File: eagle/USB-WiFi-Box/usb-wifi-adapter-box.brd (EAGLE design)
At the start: 86.4 x 52.1 mm, 12 parts

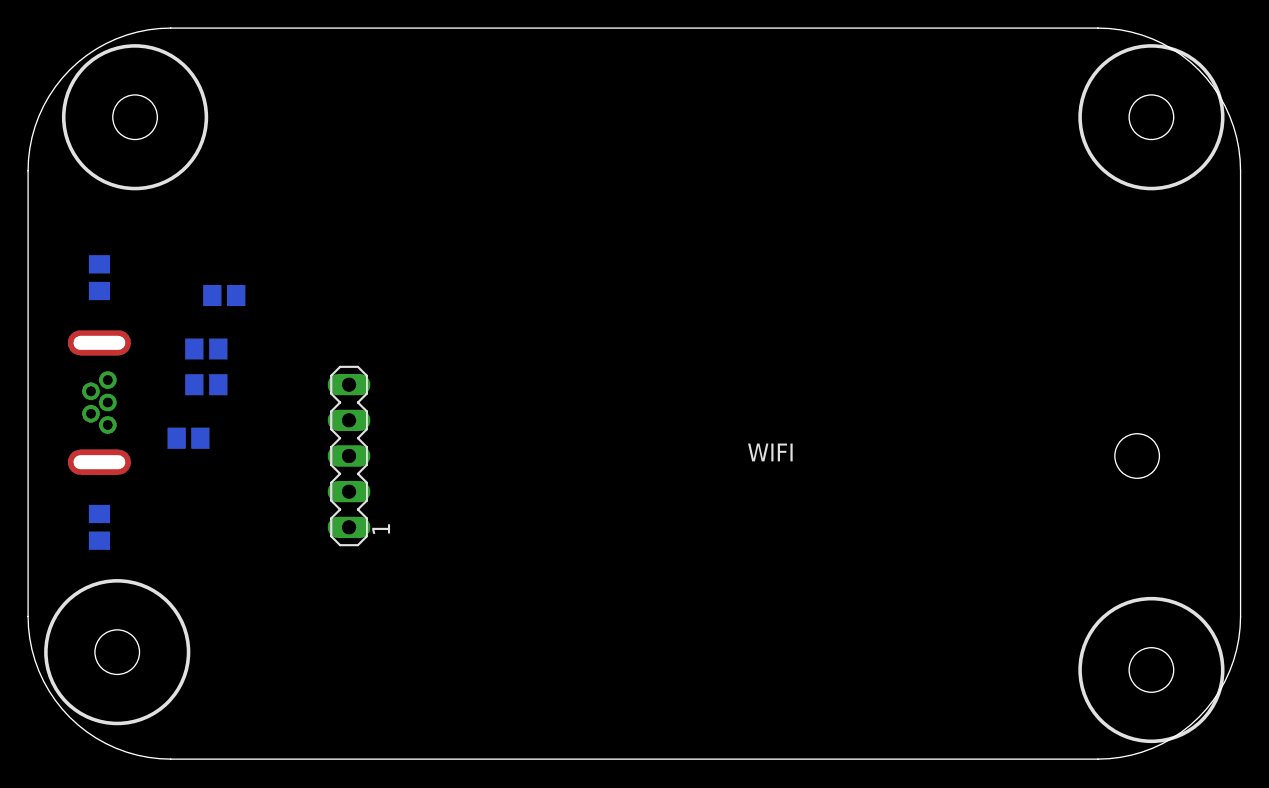
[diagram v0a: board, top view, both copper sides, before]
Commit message: board layout v1, using one wire for VCC, fixed slots in USB part
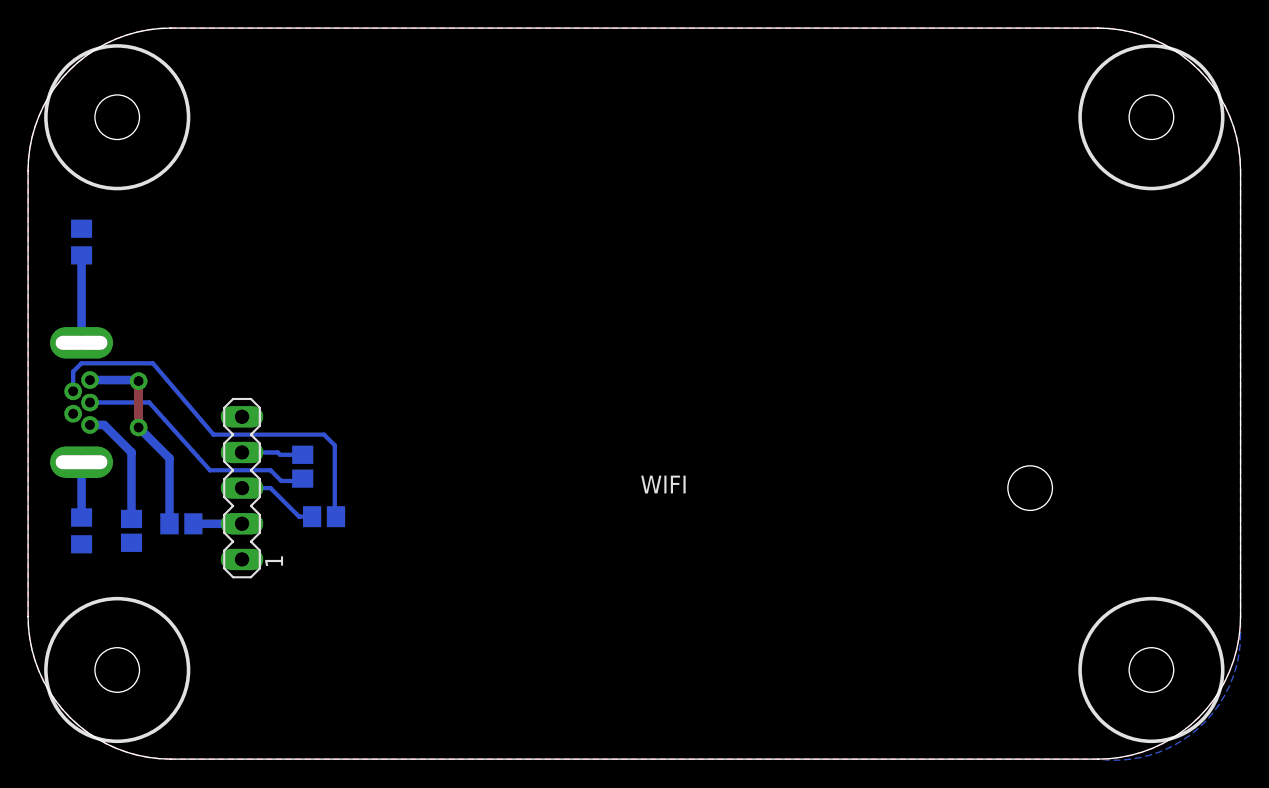
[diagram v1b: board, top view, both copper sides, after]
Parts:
- moved L1 18.0 mm to (7.37, 16.3), turned to 270 degrees
- moved L3 12.6 mm to (21.1, 17.3)
- moved L4 10.8 mm to (19.6, 20.8), turned to 90 degrees
- moved WIFI 7.96 mm to (44.5, 19.3)
- moved L2 6.12 mm to (10.9, 16.8)
- moved C1 2.84 mm to (3.81, 36.8), turned to 90 degrees
- moved C2 1.30 mm to (3.81, 16.3), turned to 270 degrees
- moved FOOT1 1.27 mm to (6.35, 45.7)
- moved FOOT2 1.27 mm to (6.35, 6.35)
- moved CONN1 1.27 mm to (3.81, 25.4)
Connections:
- net N$10 renamed D+
- net N$3 renamed D+OUT
- net N$4 renamed D-OUT
- net N$5 renamed VCC_OUT
- net N$6 renamed GNDOUT
- net N$8 renamed VCC
- net N$9 renamed D-
- removed net N$1: C2.1, CONN1.SLT2
- removed net N$7: C1.1, CONN1.SLT1
- new net SHEILDGND1: C2.1, CONN1.SHLD@2
- new net SHIELDGND2: C1.1, CONN1.SHLD@1
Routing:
- net D-OUT: track 0.00 -> 28.1 mm
- net D+OUT: track 0.00 -> 17.7 mm
- net VCC_OUT: track 0.00 -> 14.6 mm, vias 0 -> 2
- net GNDOUT: track 0.00 -> 8.50 mm
- net SHIELDGND2: track 0.00 -> 6.23 mm
- net D-: track 0.00 -> 5.83 mm
- net D+: track 0.00 -> 4.39 mm
- net SHEILDGND1: track 0.00 -> 3.94 mm
- net VCC: track 0.00 -> 3.47 mm
- added copper zone on layer 1, net GND
- added copper zone on layer 16, net GND
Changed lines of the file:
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@@
 <setting verticaltext="up"/>
 </settings>
-<grid distance="0.1" unitdist="inch" unit="inch" style="lines" multiple="1" display="yes" altdistance="0.025" altunitdist="inch" altunit="inch"/>
+<grid distance="0.01" unitdist="inch" unit="inch" style="lines" multiple="1" display="yes" altdistance="0.025" altunitdist="inch" altunit="inch"/>
 <layers>
-<layer number="1" name="Top" color="4" fill="1" visible="yes" active="yes"/>
+<layer number="1" name="Top" color="4" fill="1" visible="no" active="yes"/>
 <layer number="16" name="Bottom" color="1" fill="1" visible="yes" active="yes"/>
 <layer number="17" name="Pads" color="2" fill="1" visible="yes" active="yes"/>
@@
 <layer number="44" name="Drills" color="7" fill="1" visible="no" active="yes"/>
 <layer number="45" name="Holes" color="7" fill="1" visible="no" active="yes"/>
-<layer number="46" name="Milling" color="3" fill="1" visible="no" active="yes"/>
+<layer number="46" name="Milling" color="3" fill="1" visible="yes" active="yes"/>
 <layer number="47" name="Measures" color="7" fill="1" visible="no" active="yes"/>
 <layer number="48" name="Document" color="7" fill="1" visible="yes" active="yes"/>
@@
 </autorouter>
 <elements>
-<element name="CONN1" library="dxwifi" package="RUGGEDUSB" value="MINI-USB_SHIELD" x="5.08" y="25.4" rot="R270"/>
-<element name="L1" library="dxwifi" package="R0805" value="" x="13.97" y="33.02" rot="MR180"/>
-<element name="L4" library="dxwifi" package="R0805" value="" x="12.7" y="29.21" rot="MR0"/>
-<element name="L3" library="dxwifi" package="R0805" value="" x="12.7" y="26.67" rot="MR0"/>
-<element name="L2" library="dxwifi" package="R0805" value="" x="11.43" y="22.86" rot="MR180"/>
-<element name="C1" library="rcl" package="C0805" value="" x="5.08" y="34.29" rot="MR270"/>
-<element name="C2" library="rcl" package="C0805" value="" x="5.08" y="16.51" rot="MR90"/>
-<element name="FOOT1" library="mount-2" package="_4/.400-BARE+STD_TOOL_CLEARANCE" value="_4-BARE_MOUNTING_HOLE/.400" x="7.62" y="45.72" smashed="yes"/>
-<element name="FOOT2" library="mount-2" package="_4/.400-BARE+STD_TOOL_CLEARANCE" value="_4-BARE_MOUNTING_HOLE/.400" x="6.35" y="7.62" smashed="yes"/>
+<element name="CONN1" library="dxwifi" package="RUGGEDUSB" value="MINI-USB_SHIELD" x="3.81" y="25.4" smashed="yes" rot="R270"/>
+<element name="L1" library="dxwifi" package="R0805" value="" x="7.366" y="16.256" rot="MR270"/>
+<element name="L4" library="dxwifi" package="R0805" value="" x="19.558" y="20.828" smashed="yes" rot="MR90">
+<attribute name="NAME" x="19.05" y="23.876" size="1.27" layer="26" rot="MR90"/>
+<attribute name="VALUE" x="17.272" y="20.066" size="1.27" layer="28" rot="MR90"/>
+</element>
+<element name="L3" library="dxwifi" package="R0805" value="" x="21.082" y="17.272" smashed="yes" rot="MR0">
+<attribute name="NAME" x="25.4" y="16.764" size="1.27" layer="26" rot="MR0"/>
+<attribute name="VALUE" x="21.844" y="14.986" size="1.27" layer="28" rot="MR0"/>
+</element>
+<element name="L2" library="dxwifi" package="R0805" value="" x="10.922" y="16.764" rot="MR180"/>
+<element name="C1" library="rcl" package="C0805" value="" x="3.81" y="36.83" rot="MR90"/>
+<element name="C2" library="rcl" package="C0805" value="" x="3.81" y="16.256" rot="MR270"/>
+<element name="FOOT1" library="mount-2" package="_4/.400-BARE+STD_TOOL_CLEARANCE" value="_4-BARE_MOUNTING_HOLE/.400" x="6.35" y="45.72" smashed="yes"/>
+<element name="FOOT2" library="mount-2" package="_4/.400-BARE+STD_TOOL_CLEARANCE" value="_4-BARE_MOUNTING_HOLE/.400" x="6.35" y="6.35" smashed="yes"/>
 <element name="FOOT3" library="mount-2" package="_4/.400-BARE+STD_TOOL_CLEARANCE" value="_4-BARE_MOUNTING_HOLE/.400" x="80.01" y="6.35" smashed="yes"/>
 <element name="FOOT4" library="mount-2" package="_4/.400-BARE+STD_TOOL_CLEARANCE" value="_4-BARE_MOUNTING_HOLE/.400" x="80.01" y="45.72" smashed="yes"/>
-<element name="WIFI" library="dxwifi" package="ZCN-722M" value="ZCN-722M" x="52.07" y="21.59"/>
+<element name="WIFI" library="dxwifi" package="ZCN-722M" value="ZCN-722M" x="44.45" y="19.304"/>
 </elements>
 <signals>
-<signal name="N$3">
+<signal name="D+OUT">
 <contactref element="CONN1" pad="3"/>
 <contactref element="L4" pad="1"/>
-<wire x1="5.68" y1="25.4" x2="13.55" y2="29.21" width="0" layer="19" extent="1-1"/>
-</signal>
-<signal name="N$4">
+<wire x1="4.41" y1="25.4" x2="8.636" y2="25.4" width="0.3048" layer="16"/>
+<wire x1="8.636" y1="25.4" x2="12.954" y2="20.574" width="0.3048" layer="16"/>
+<wire x1="12.954" y1="20.574" x2="17.272" y2="20.574" width="0.3048" layer="16"/>
+<wire x1="17.272" y1="20.574" x2="18.034" y2="19.812" width="0.3048" layer="16"/>
+<wire x1="18.034" y1="19.812" x2="19.392" y2="19.812" width="0.3048" layer="16"/>
+<wire x1="19.392" y1="19.812" x2="19.558" y2="19.978" width="0.3048" layer="16"/>
+</signal>
+<signal name="D-OUT">
 <contactref element="CONN1" pad="2"/>
 <contactref element="L3" pad="1"/>
-<wire x1="4.48" y1="26.2" x2="13.55" y2="26.67" width="0" layer="19" extent="1-1"/>
-</signal>
-<signal name="N$5">
+<wire x1="3.21" y1="26.2" x2="3.21" y2="27.594" width="0.3048" layer="16"/>
+<wire x1="3.21" y1="27.594" x2="3.81" y2="28.194" width="0.3048" layer="16"/>
+<wire x1="3.81" y1="28.194" x2="8.89" y2="28.194" width="0.3048" layer="16"/>
+<wire x1="8.89" y1="28.194" x2="13.208" y2="23.114" width="0.3048" layer="16"/>
+<wire x1="13.208" y1="23.114" x2="21.082" y2="23.114" width="0.3048" layer="16"/>
+<wire x1="21.082" y1="23.114" x2="21.844" y2="22.352" width="0.3048" layer="16"/>
+<wire x1="21.844" y1="22.352" x2="21.844" y2="17.36" width="0.3048" layer="16"/>
+<wire x1="21.844" y1="17.36" x2="21.932" y2="17.272" width="0.3048" layer="16"/>
+</signal>
+<signal name="VCC_OUT">
 <contactref element="CONN1" pad="1"/>
 <contactref element="L2" pad="1"/>
-<wire x1="5.68" y1="27" x2="10.58" y2="22.86" width="0" layer="19" extent="1-1"/>
+<wire x1="10.072" y1="16.764" x2="10.072" y2="21.424" width="0.6096" layer="16"/>
+<wire x1="10.072" y1="21.424" x2="7.874" y2="23.622" width="0.6096" layer="16"/>
+<via x="7.874" y="23.622" extent="1-16" drill="0.7" diameter="1.27"/>
+<wire x1="7.874" y1="23.622" x2="7.874" y2="26.924" width="0.6096" layer="1"/>
+<via x="7.874" y="26.924" extent="1-16" drill="0.7" diameter="1.27"/>
+<wire x1="7.874" y1="26.924" x2="7.798" y2="27" width="0.6096" layer="16"/>
+<wire x1="7.798" y1="27" x2="4.41" y2="27" width="0.6096" layer="16"/>
 </signal>
 <signal name="GND">
@@
 <contactref element="L1" pad="2"/>
 <contactref element="WIFI" pad="5"/>
-<wire x1="14.82" y1="33.02" x2="22.86" y2="26.67" width="0" layer="19" extent="1-1"/>
-<wire x1="5.08" y1="17.46" x2="14.82" y2="33.02" width="0" layer="19" extent="1-1"/>
-<wire x1="5.08" y1="33.34" x2="5.08" y2="17.46" width="0" layer="19" extent="1-1"/>
-</signal>
-<signal name="N$6">
+<polygon width="0.4064" layer="16" orphans="yes">
+<vertex x="0" y="41.91" curve="-90"/>
+<vertex x="10.16" y="52.07"/>
+<vertex x="76.2" y="52.07" curve="-90"/>
+<vertex x="86.36" y="41.91"/>
+<vertex x="86.36" y="8.89" curve="-97.62815"/>
+<vertex x="76.2" y="0"/>
+<vertex x="10.16" y="0" curve="-90"/>
+<vertex x="0" y="10.16"/>
+</polygon>
+<polygon width="0.4064" layer="1">
+<vertex x="0" y="41.91" curve="-90"/>
+<vertex x="10.16" y="52.07"/>
+<vertex x="76.2" y="52.07" curve="-90"/>
+<vertex x="86.36" y="41.91"/>
+<vertex x="86.36" y="10.16" curve="-90"/>
+<vertex x="76.2" y="0"/>
+<vertex x="10.16" y="0" curve="-90"/>
+<vertex x="0" y="10.16"/>
+</polygon>
+</signal>
+<signal name="GNDOUT">
 <contactref element="CONN1" pad="5"/>
 <contactref element="L1" pad="1"/>
-<wire x1="13.12" y1="33.02" x2="5.68" y2="23.8" width="0" layer="19" extent="1-1"/>
-</signal>
-<signal name="N$1">
-<contactref element="CONN1" pad="SLT2"/>
+<wire x1="4.41" y1="23.8" x2="5.41" y2="23.8" width="0.6096" layer="16"/>
+<wire x1="5.41" y1="23.8" x2="7.366" y2="21.844" width="0.6096" layer="16"/>
+<wire x1="7.366" y1="21.844" x2="7.366" y2="17.106" width="0.6096" layer="16"/>
+</signal>
+<signal name="SHEILDGND1">
+<contactref element="CONN1" pad="SHLD@2"/>
 <contactref element="C2" pad="1"/>
-<wire x1="5.08" y1="15.56" x2="5.08" y2="21.15" width="0" layer="19" extent="1-1"/>
-</signal>
-<signal name="N$7">
-<contactref element="CONN1" pad="SLT1"/>
+<wire x1="3.81" y1="17.206" x2="3.81" y2="21.15" width="0.6096" layer="16"/>
+</signal>
+<signal name="SHIELDGND2">
+<contactref element="CONN1" pad="SHLD@1"/>
 <contactref element="C1" pad="1"/>
-<wire x1="5.08" y1="35.24" x2="5.08" y2="29.65" width="0" layer="19" extent="1-1"/>
-</signal>
-<signal name="N$8">
+<wire x1="3.81" y1="35.88" x2="3.81" y2="29.65" width="0.6096" layer="16"/>
+</signal>
+<signal name="VCC">
 <contactref element="L2" pad="2"/>
 <contactref element="WIFI" pad="2"/>
-<wire x1="12.28" y1="22.86" x2="22.86" y2="19.05" width="0" layer="19" extent="1-1"/>
-</signal>
-<signal name="N$9">
+<wire x1="11.772" y1="16.764" x2="15.24" y2="16.764" width="0.6096" layer="16"/>
+</signal>
+<signal name="D-">
 <contactref element="L3" pad="2"/>
 <contactref element="WIFI" pad="3"/>
-<wire x1="11.85" y1="26.67" x2="22.86" y2="21.59" width="0" layer="19" extent="1-1"/>
-</signal>
-<signal name="N$10">
+<wire x1="20.232" y1="17.272" x2="19.304" y2="17.272" width="0.3048" layer="16"/>
+<wire x1="19.304" y1="17.272" x2="17.272" y2="19.304" width="0.3048" layer="16"/>
+<wire x1="17.272" y1="19.304" x2="15.24" y2="19.304" width="0.3048" layer="16"/>
+</signal>
+<signal name="D+">
 <contactref element="L4" pad="2"/>
 <contactref element="WIFI" pad="4"/>
-<wire x1="11.85" y1="29.21" x2="22.86" y2="24.13" width="0" layer="19" extent="1-1"/>
+<wire x1="19.558" y1="21.678" x2="17.946" y2="21.678" width="0.3048" layer="16"/>
+<wire x1="17.946" y1="21.678" x2="17.78" y2="21.844" width="0.3048" layer="16"/>
+<wire x1="17.78" y1="21.844" x2="15.24" y2="21.844" width="0.3048" layer="16"/>
 </signal>
 </signals>

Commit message: fix routing issues
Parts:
- added TP1: PTR1PAD1-13, testpad:P1-13
- moved L3 16.4 mm to (8.64, 27.9), turned to 180 degrees
- moved L4 11.2 mm to (8.38, 21.6), turned to 180 degrees
- moved L1 10.4 mm to (1.27, 24.6), turned to 90 degrees
- moved L2 9.60 mm to (7.62, 25.8)
- moved C1 3.94 mm to (3.81, 32.9)
- moved C2 1.65 mm to (3.81, 17.9)
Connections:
- new net N$1: TP1.TP, WIFI.1
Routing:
- net D-OUT: track 28.1 -> 6.23 mm
- net D-: track 5.83 -> 18.6 mm
- net D+OUT: track 17.7 -> 5.64 mm
- net VCC: track 3.47 -> 15.4 mm, vias 0 -> 2
- net VCC_OUT: track 14.6 -> 2.86 mm, vias 2 -> 0
- net N$1: track 0.00 -> 6.86 mm
- net GNDOUT: track 8.50 -> 4.28 mm
- net SHIELDGND2: track 6.23 -> 2.29 mm
- net D+: track 4.39 -> 6.11 mm
- net SHEILDGND1: track 3.94 -> 2.29 mm

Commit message: minor fixes, values of caps
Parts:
- C1, C2: value (none) -> 0.1u
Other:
- board text added: "Dimentions of Altoid box"
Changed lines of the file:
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@@
 <setting verticaltext="up"/>
 </settings>
-<grid distance="0.01" unitdist="inch" unit="inch" style="lines" multiple="1" display="yes" altdistance="0.025" altunitdist="inch" altunit="inch"/>
+<grid distance="0.1" unitdist="inch" unit="inch" style="lines" multiple="1" display="yes" altdistance="0.025" altunitdist="inch" altunit="inch"/>
 <layers>
 <layer number="1" name="Top" color="4" fill="1" visible="no" active="yes"/>
@@
 <layer number="45" name="Holes" color="7" fill="1" visible="no" active="yes"/>
 <layer number="46" name="Milling" color="3" fill="1" visible="yes" active="yes"/>
-<layer number="47" name="Measures" color="7" fill="1" visible="no" active="yes"/>
+<layer number="47" name="Measures" color="7" fill="1" visible="yes" active="yes"/>
 <layer number="48" name="Document" color="7" fill="1" visible="yes" active="yes"/>
 <layer number="49" name="Reference" color="7" fill="1" visible="yes" active="yes"/>
@@
 <wire x1="10.16" y1="-2.54" x2="-2.54" y2="10.16" width="0.4064" layer="48" curve="-90"/>
 <wire x1="-2.54" y1="10.16" x2="-2.54" y2="41.91" width="0.4064" layer="48"/>
+<dimension x1="-2.54" y1="41.91" x2="88.9" y2="41.91" x3="43.18" y3="60.96" textsize="1.778" layer="47" unit="inch"/>
+<dimension x1="76.2" y1="-2.54" x2="76.2" y2="54.61" x3="-10.16" y3="26.035" textsize="1.778" layer="47" unit="inch"/>
+<text x="-10.16" y="58.42" size="1.778" layer="47">Dimentions of Altoid box</text>
 </plain>
 <attributes>
@@
 </element>
 <element name="L2" library="dxwifi" package="R0805" value="" x="7.62" y="25.781" rot="MR180"/>
-<element name="C1" library="rcl" package="C0805" value="" x="3.81" y="32.893" rot="MR90"/>
-<element name="C2" library="rcl" package="C0805" value="" x="3.81" y="17.907" rot="MR270"/>
+<element name="C1" library="rcl" package="C0805" value="0.1u" x="3.81" y="32.893" rot="MR90"/>
+<element name="C2" library="rcl" package="C0805" value="0.1u" x="3.81" y="17.907" rot="MR270"/>
 <element name="FOOT1" library="mount-2" package="_4/.400-BARE+STD_TOOL_CLEARANCE" value="_4-BARE_MOUNTING_HOLE/.400" x="6.35" y="45.72" smashed="yes"/>
 <element name="FOOT2" library="mount-2" package="_4/.400-BARE+STD_TOOL_CLEARANCE" value="_4-BARE_MOUNTING_HOLE/.400" x="6.35" y="6.35" smashed="yes"/>
@@
 <vertex x="76.2" y="52.07" curve="-90"/>
 <vertex x="86.36" y="41.91"/>
-<vertex x="86.36" y="8.89" curve="-97.62815"/>
+<vertex x="86.36" y="10.16" curve="-90"/>
 <vertex x="76.2" y="0"/>
 <vertex x="10.16" y="0" curve="-90"/>
